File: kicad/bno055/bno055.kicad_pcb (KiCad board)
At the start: 2 copper layers, 31 x 42 mm, 39 parts, among them J1 USB4125-GF-A_REVA, J2 PinHeader_2x03_P2.54mm_Vertic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, J3 PinHeader_1x05_P2.54mm_Vertic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, J4 PinHeader_1x02_P2.54mm_Vertic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, SW1 SW_SPDT, U1 dfn-8_wide, U2 BQ297xy, U3 CSD85302L, U4 NCP177BMX330TCG, U5 BMI160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

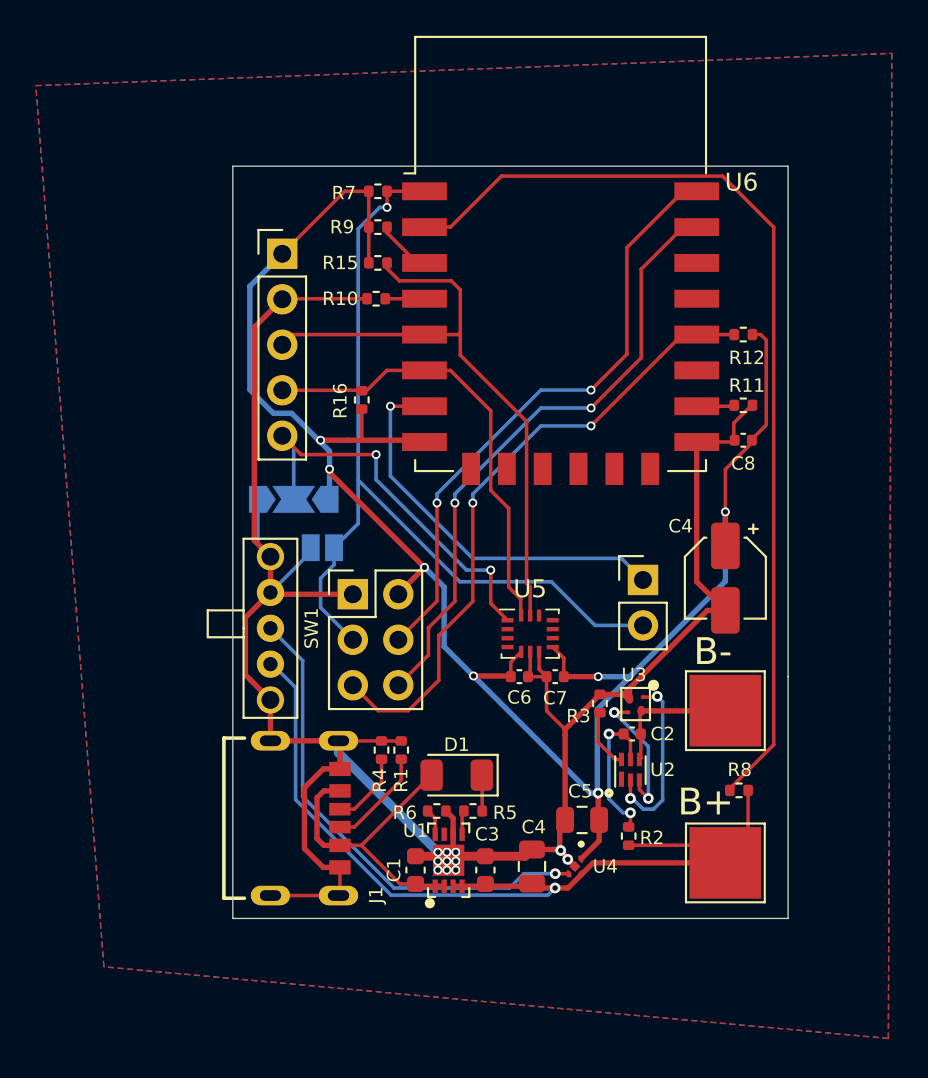
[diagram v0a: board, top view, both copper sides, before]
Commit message: added bno055 support unfortunately some componts ha to be mouted on the back as they were to lage for the front
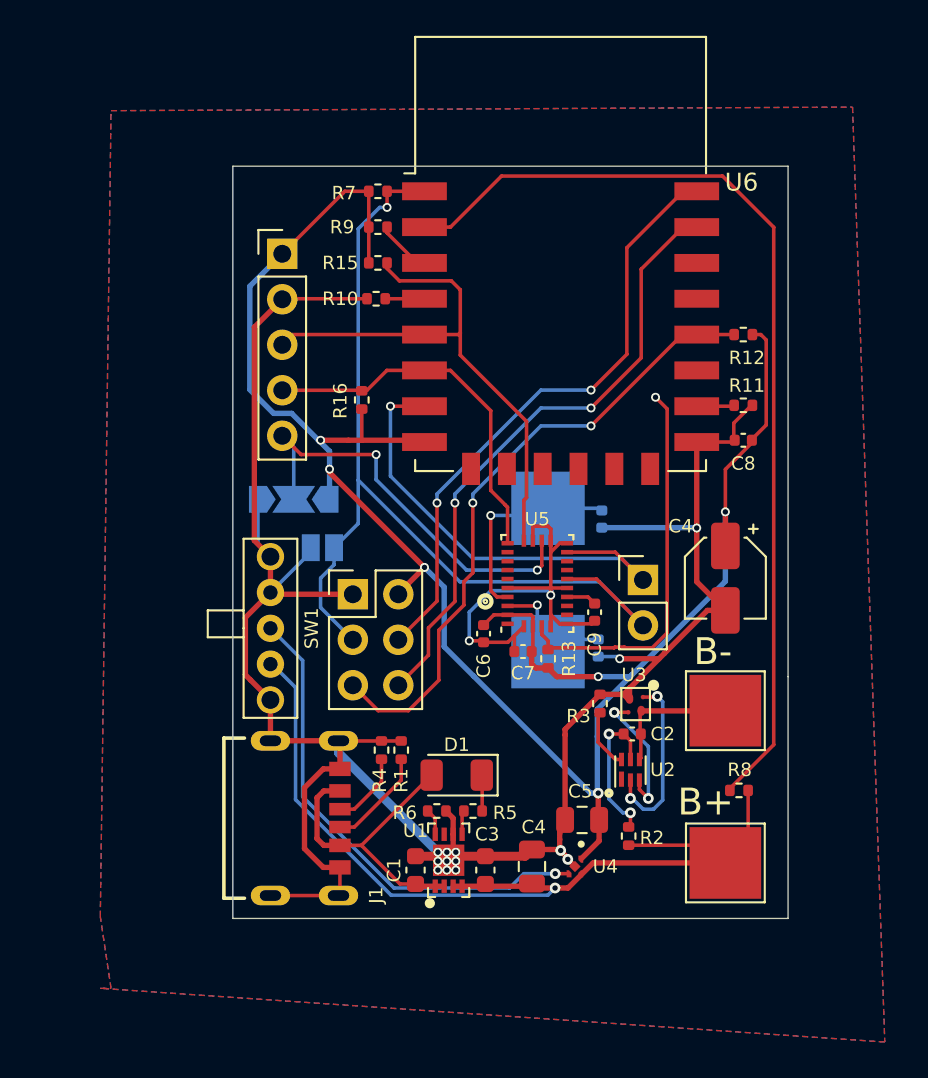
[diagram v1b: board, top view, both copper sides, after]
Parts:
- added C10: 15pf, Capacitor_SMD:C_0402_1005Metric, B.Cu at (129.6, 87.2)
- added C11: 15pf, Capacitor_SMD:C_0402_1005Metric, B.Cu at (129.4, 94.4)
- added C9: 100nf, Capacitor_SMD:C_0402_1005Metric, F.Cu at (129.2, 92.4)
- added R13: 10k, Resistor_SMD:R_0402_1005Metric, F.Cu at (126.6, 95.0)
- added Y1: MC-405 32.0000K-R3: PURE SN, Crystal:Crystal_SMD_SeikoEpson_MC405-2Pin_9.6x4.1mm, B.Cu at (126.6, 90.6)
- U5: value BMI160 -> BNO055; footprint Package_LGA:Bosch_LGA-14_3x2.5mm_P0.5mm -> Package_LGA:LGA-28_5.2x3.8mm_P0.5mm
- moved C6 3.12 mm to (123.0, 93.6), turned to 90 degrees
- moved U5 2.83 mm to (126.0, 90.8), turned to 90 degrees
- moved C7 2.28 mm to (125.2, 94.6)
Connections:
- C1 pad 1: +5V -> GND
- C3 pad 2: +BATT -> GND
- R5 pad 1: /CH_STAT -> Net-(D1-Pad1)
- R5 pad 2: Net-(D1-Pad1) -> /CH_STAT
- U4 pad 5: (no net) -> GND
- U5 pad 1: /ADDRESS -> unconnected-(U5-Pad1)
- U5 pad 10: unconnected-(U5-Pad10) -> GND
- U5 pad 11: unconnected-(U5-Pad11) -> /RESET
- U5 pad 12: +3.3V -> unconnected-(U5-Pad12)
- U5 pad 13: /H_SCL -> unconnected-(U5-Pad13)
- U5 pad 14: /H_SDA -> /INT
- U5 pad 2: unconnected-(U5-Pad2) -> GND
- U5 pad 3: unconnected-(U5-Pad3) -> +3.3V
- U5 pad 4: unconnected-(U5-Pad4) -> /BOOTN
- U5 pad 5: +3.3V -> GND
- U5 pad 7: GND -> unconnected-(U5-Pad7)
- U5 pad 8: +3.3V -> unconnected-(U5-Pad8)
- U5 pad 9: unconnected-(U5-Pad9) -> /cap
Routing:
- net GND: track 130.3 -> 157.4 mm, vias 11 -> 15
- net /BOOTN: track 0.00 -> 21.9 mm, vias 0 -> 1
- net Net-(C10-Pad1): track 0.00 -> 11.7 mm, vias 0 -> 1
- net Net-(C11-Pad1): track 0.00 -> 7.61 mm, vias 0 -> 1
- net /RESET: track 49.6 -> 54.9 mm
- net /INT: track 22.3 -> 27.2 mm
- net /H_SDA: track 25.2 -> 20.8 mm
- net /H_SCL: track 34.9 -> 30.7 mm
- net +3.3V: track 112.8 -> 115.0 mm, vias 7 -> 6
- net /cap: track 0.00 -> 1.69 mm
- net CH_PROG: track 1.47 -> 0.00 mm
- net /CH_PROG: track 0.00 -> 1.47 mm
- net Net-(D1-Pad1): track 2.01 -> 3.35 mm
- net /CH_STAT: track 1.34 -> 0.00 mm
- net /ADDRESS: track 22.6 -> 23.7 mm
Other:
- board text removed: "BMI ADDRESS"
- board text removed: "BMI PINS"
